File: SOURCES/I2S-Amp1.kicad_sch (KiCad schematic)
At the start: 37 parts, among them P10 CONN_01X02, P17 TST, P24 TST, P25 TST, P26 TST, P9 CONN_01X02, U3 SN74LVC14ADG4, U4 TAS5760MDCAR

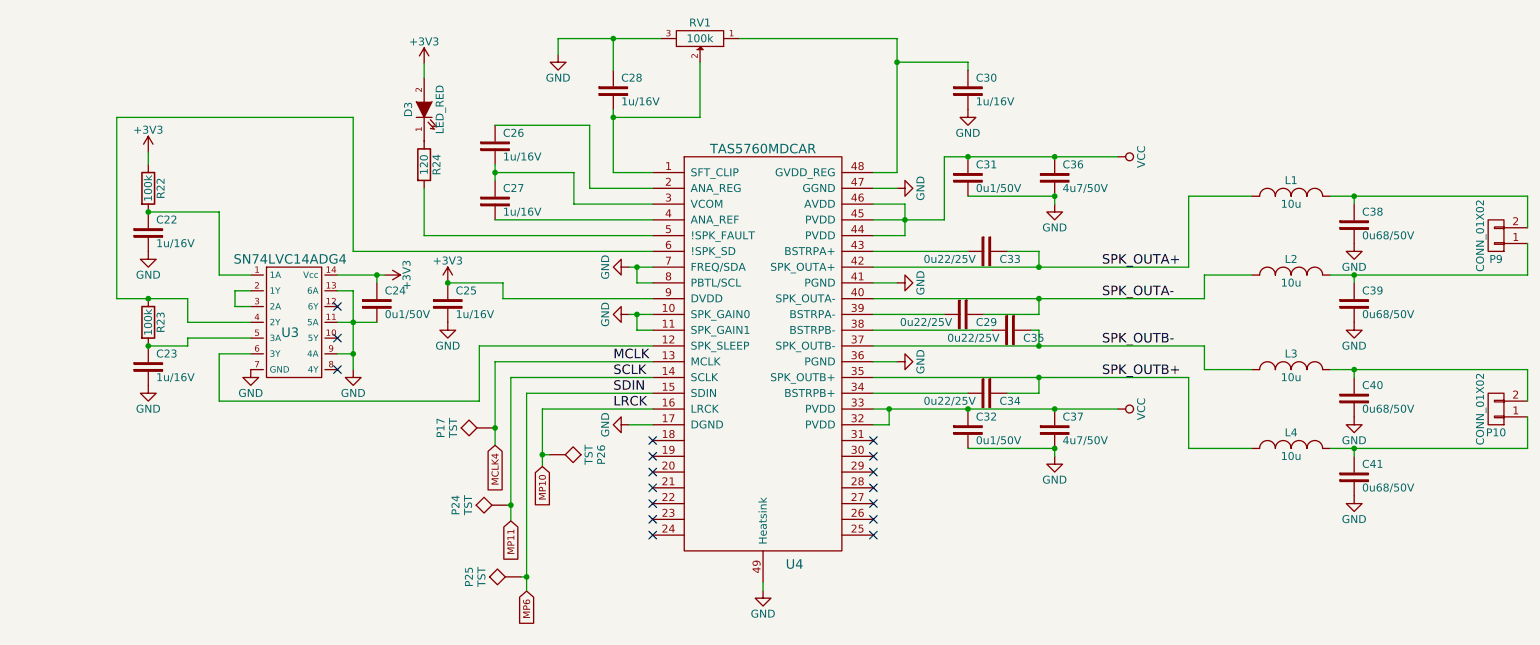
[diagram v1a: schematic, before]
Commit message: Removed redundant 7414 and pot, rerouted a bit.
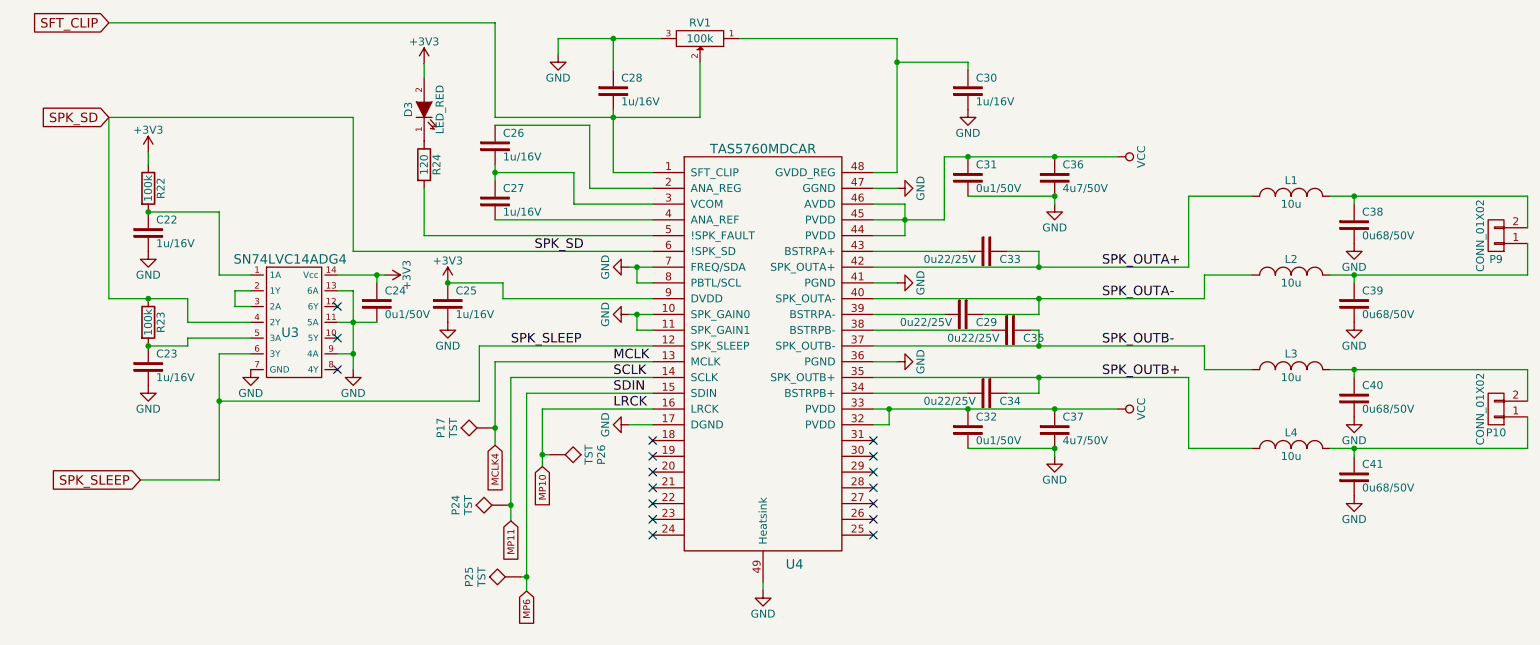
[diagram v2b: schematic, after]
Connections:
- net SFT_CLIP: now reaches C28.2, RV1.2, U4.1 (SFT_CLIP)
- net SPK_SD: now reaches R23.1, U3.4 (2Y), U4.6 (!SPK_SD)
- net SPK_SLEEP: now reaches U3.6 (3Y), U4.12 (SPK_SLEEP)
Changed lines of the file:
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@@
   (junction (at 190.5 81.28) (diameter 0) (color 0 0 0 0)
+  )
+  (junction (at 58.42 85.09) (diameter 0) (color 0 0 0 0)
   )
   (junction (at 80.01 77.47) (diameter 0) (color 0 0 0 0)
@@
     (stroke (width 0) (type default))
   )
+  (wire (pts (xy 40.64 24.13) (xy 102.87 24.13))
+    (stroke (width 0) (type default))
+  )
   (wire (pts (xy 167.64 26.67) (xy 167.64 30.48))
     (stroke (width 0) (type default))
@@
     (stroke (width 0) (type default))
   )
+  (wire (pts (xy 102.87 39.37) (xy 121.92 39.37))
+    (stroke (width 0) (type default))
+  )
   (wire (pts (xy 179.07 83.82) (xy 163.83 83.82))
     (stroke (width 0) (type default))
@@
     (stroke (width 0) (type default))
   )
+  (wire (pts (xy 58.42 97.79) (xy 58.42 85.09))
+    (stroke (width 0) (type default))
+  )
   (wire (pts (xy 175.26 45.72) (xy 179.07 45.72))
     (stroke (width 0) (type default))
@@
     (stroke (width 0) (type default))
   )
-  (wire (pts (xy 41.91 68.58) (xy 41.91 39.37))
+  (wire (pts (xy 40.64 68.58) (xy 40.64 39.37))
     (stroke (width 0) (type default))
   )
@@
     (stroke (width 0) (type default))
   )
-  (wire (pts (xy 41.91 68.58) (xy 46.99 68.58))
+  (wire (pts (xy 40.64 68.58) (xy 46.99 68.58))
     (stroke (width 0) (type default))
   )
@@
     (stroke (width 0) (type default))
   )
+  (wire (pts (xy 102.87 24.13) (xy 102.87 39.37))
+    (stroke (width 0) (type default))
+  )
   (wire (pts (xy 102.87 55.88) (xy 128.27 55.88))
     (stroke (width 0) (type default))
@@
     (stroke (width 0) (type default))
   )
-  (wire (pts (xy 41.91 39.37) (xy 80.01 39.37))
+  (wire (pts (xy 40.64 39.37) (xy 80.01 39.37))
     (stroke (width 0) (type default))
   )
@@
     (stroke (width 0) (type default))
   )
+  (wire (pts (xy 45.72 97.79) (xy 58.42 97.79))
+    (stroke (width 0) (type default))
+  )
   (wire (pts (xy 241.3 64.77) (xy 241.3 66.04))
     (stroke (width 0) (type default))
@@
     (stroke (width 0) (type default))
   )
-  (label "SPK_OUTB-" (at 200.66 76.2 0)
-    (effects (font (size 1.524 1.524)) (justify left bottom))
-  )
-  (label "SDIN" (at 121.92 83.82 0)
-    (effects (font (size 1.524 1.524)) (justify left bottom))
-  )
-  (label "SPK_OUTA-" (at 200.66 68.58 0)
-    (effects (font (size 1.524 1.524)) (justify left bottom))
-  )
-  (label "SPK_OUTA+" (at 200.66 63.5 0)
-    (effects (font (size 1.524 1.524)) (justify left bottom))
-  )
-  (label "SCLK" (at 121.92 81.28 0)
-    (effects (font (size 1.524 1.524)) (justify left bottom))
-  )
-  (label "LRCK" (at 121.92 86.36 0)
-    (effects (font (size 1.524 1.524)) (justify left bottom))
-  )
-  (label "SPK_OUTB+" (at 200.66 81.28 0)
-    (effects (font (size 1.524 1.524)) (justify left bottom))
-  )
-  (label "MCLK" (at 121.92 78.74 0)
+  (label "SPK_OUTB-" (at 200.66 76.2 0) (fields_autoplaced)
+    (effects (font (size 1.524 1.524)) (justify left bottom))
+  )
+  (label "SDIN" (at 121.92 83.82 0) (fields_autoplaced)
+    (effects (font (size 1.524 1.524)) (justify left bottom))
+  )
+  (label "SPK_SD" (at 109.22 60.96 0) (fields_autoplaced)
+    (effects (font (size 1.524 1.524)) (justify left bottom))
+  )
+  (label "SPK_SLEEP" (at 105.41 76.2 0) (fields_autoplaced)
+    (effects (font (size 1.524 1.524)) (justify left bottom))
+  )
+  (label "SPK_OUTA-" (at 200.66 68.58 0) (fields_autoplaced)
+    (effects (font (size 1.524 1.524)) (justify left bottom))
+  )
+  (label "SPK_OUTA+" (at 200.66 63.5 0) (fields_autoplaced)
+    (effects (font (size 1.524 1.524)) (justify left bottom))
+  )
+  (label "SCLK" (at 121.92 81.28 0) (fields_autoplaced)
+    (effects (font (size 1.524 1.524)) (justify left bottom))
+  )
+  (label "LRCK" (at 121.92 86.36 0) (fields_autoplaced)
+    (effects (font (size 1.524 1.524)) (justify left bottom))
+  )
+  (label "SPK_OUTB+" (at 200.66 81.28 0) (fields_autoplaced)
+    (effects (font (size 1.524 1.524)) (justify left bottom))
+  )
+  (label "MCLK" (at 121.92 78.74 0) (fields_autoplaced)
     (effects (font (size 1.524 1.524)) (justify left bottom))
   )
@@
     )
   )
+  (global_label "SPK_SLEEP" (shape input) (at 45.72 97.79 180) (fields_autoplaced)
+    (effects (font (size 1.524 1.524)) (justify right))
+    (property "Intersheetrefs" "${INTERSHEET_REFS}" (at 30.2958 97.79 0)
+      (effects (font (size 1.27 1.27)) (justify right) hide)
+    )
+  )
+  (global_label "SFT_CLIP" (shape input) (at 40.64 24.13 180) (fields_autoplaced)
+    (effects (font (size 1.524 1.524)) (justify right))
+    (property "Intersheetrefs" "${INTERSHEET_REFS}" (at 27.7559 24.13 0)
+      (effects (font (size 1.27 1.27)) (justify right) hide)
+    )
+  )
+  (global_label "SPK_SD" (shape input) (at 40.64 39.37 180) (fields_autoplaced)
+    (effects (font (size 1.524 1.524)) (justify right))
+    (property "Intersheetrefs" "${INTERSHEET_REFS}" (at 29.2073 39.37 0)
+      (effects (font (size 1.27 1.27)) (justify right) hide)
+    )
+  )

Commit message: Removed ArduinoPort, Changed Power Supply. Rerouting and stuff.
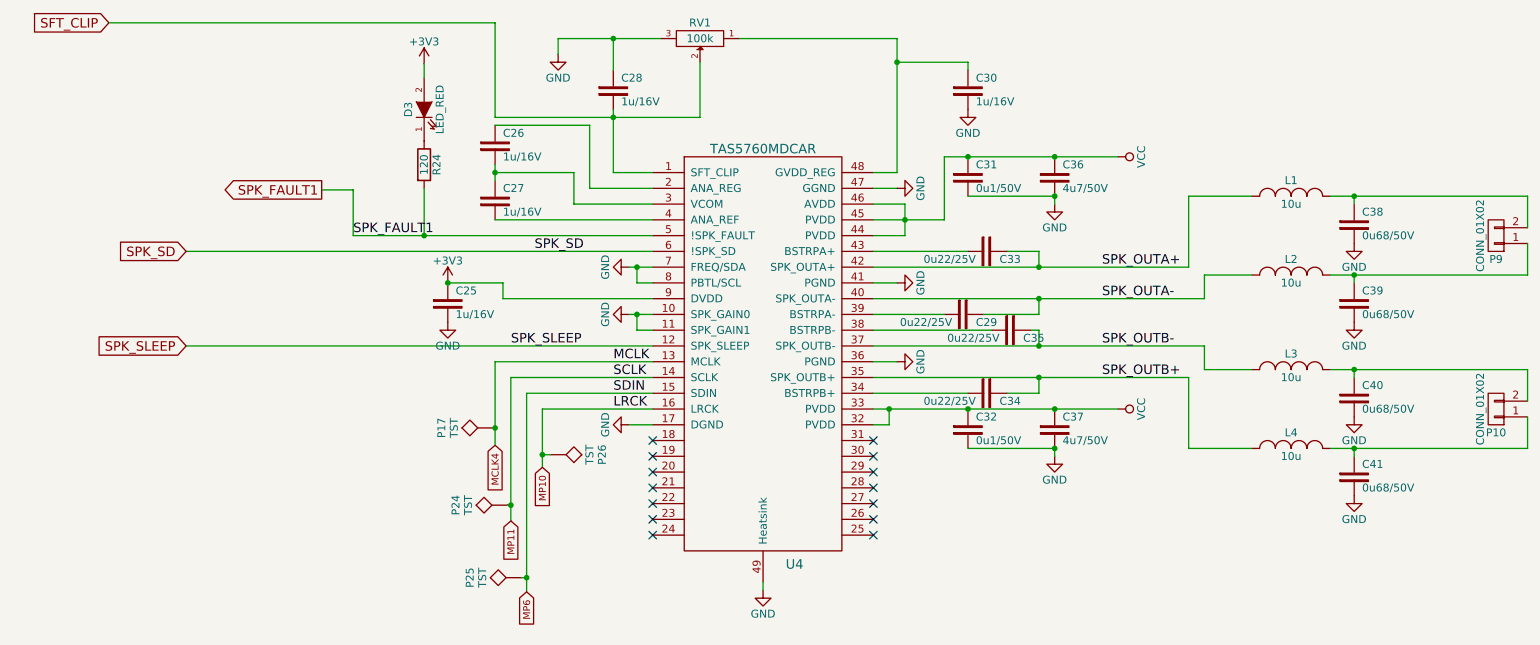
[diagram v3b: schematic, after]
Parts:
- removed C22, C23: 1u/16V, fdsp_capacitor:C_1206_HandSoldering, symbol MyLibrary:Capacitor
- removed C24: 0u1/50V, fdsp_capacitor:C_1206_HandSoldering, symbol MyLibrary:Capacitor
- removed R22, R23: 100k, fdsp_resistor:R_1206_HandSoldering, symbol smd_aio-rescue:R
- removed U3: SN74LVC14ADG4, Housings_SOIC:SOIC-14_3.9x8.7mm_Pitch1.27mm, symbol MyLibrary:SN74LVC14ADG4
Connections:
- net SPK_FAULT1: now reaches R24.2, U4.5 (!SPK_FAULT)
- no-connect marks 17 -> 14

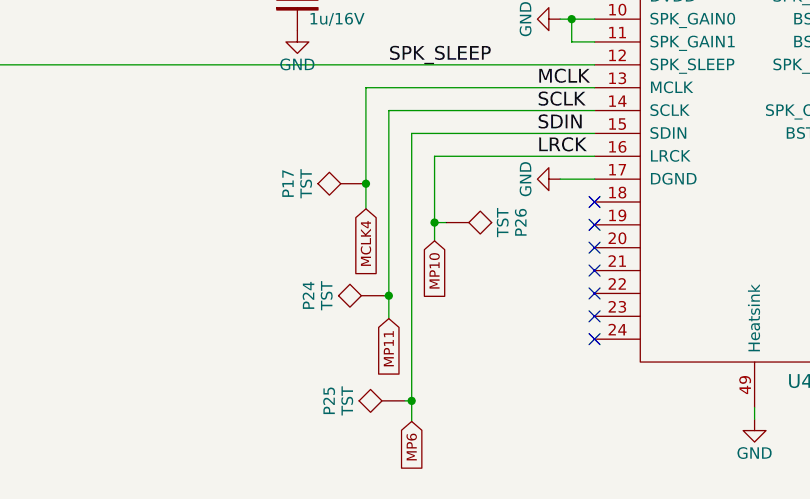
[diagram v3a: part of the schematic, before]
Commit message: Added power down detection.
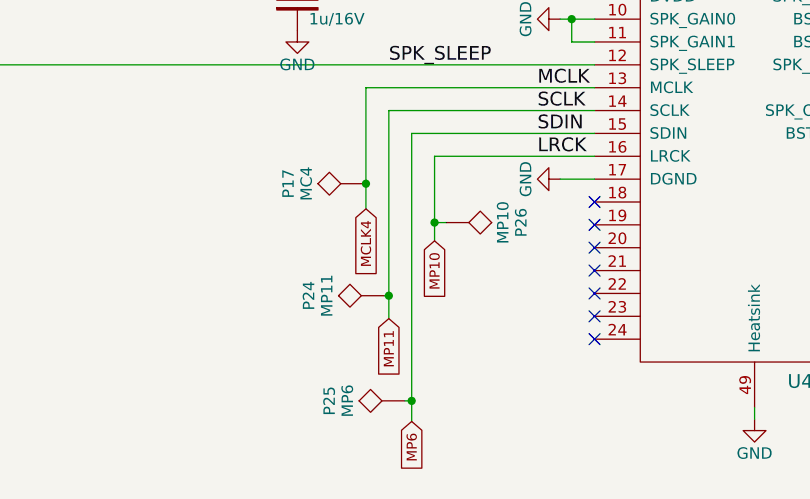
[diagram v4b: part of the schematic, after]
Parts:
- P17: value TST -> MC4
- P24: value TST -> MP11
- P25: value TST -> MP6
- P26: value TST -> MP10
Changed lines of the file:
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@@
       (effects (font (size 1.27 1.27)) (justify bottom))
     )
-    (property "Value" "TST" (at 96.266 89.408 0)
+    (property "Value" "MC4" (at 96.266 89.408 0)
       (effects (font (size 1.27 1.27)))
     )
@@
       (effects (font (size 1.27 1.27)) (justify bottom))
     )
-    (property "Value" "TST" (at 98.552 101.854 0)
+    (property "Value" "MP11" (at 98.552 101.854 0)
       (effects (font (size 1.27 1.27)))
     )
@@
       (effects (font (size 1.27 1.27)) (justify bottom))
     )
-    (property "Value" "TST" (at 100.838 113.538 0)
+    (property "Value" "MP6" (at 100.838 113.538 0)
       (effects (font (size 1.27 1.27)))
     )
@@
       (effects (font (size 1.27 1.27)) (justify bottom))
     )
-    (property "Value" "TST" (at 118.11 93.726 0)
+    (property "Value" "MP10" (at 118.11 93.726 0)
       (effects (font (size 1.27 1.27)))
     )

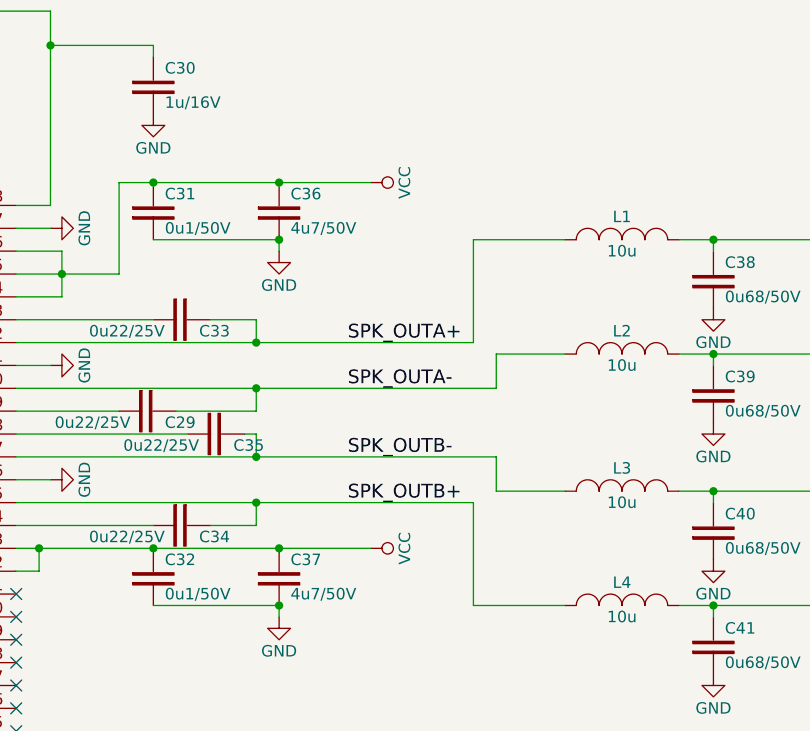
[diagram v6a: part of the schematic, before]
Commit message: Fixed Vin/Vcc issue.
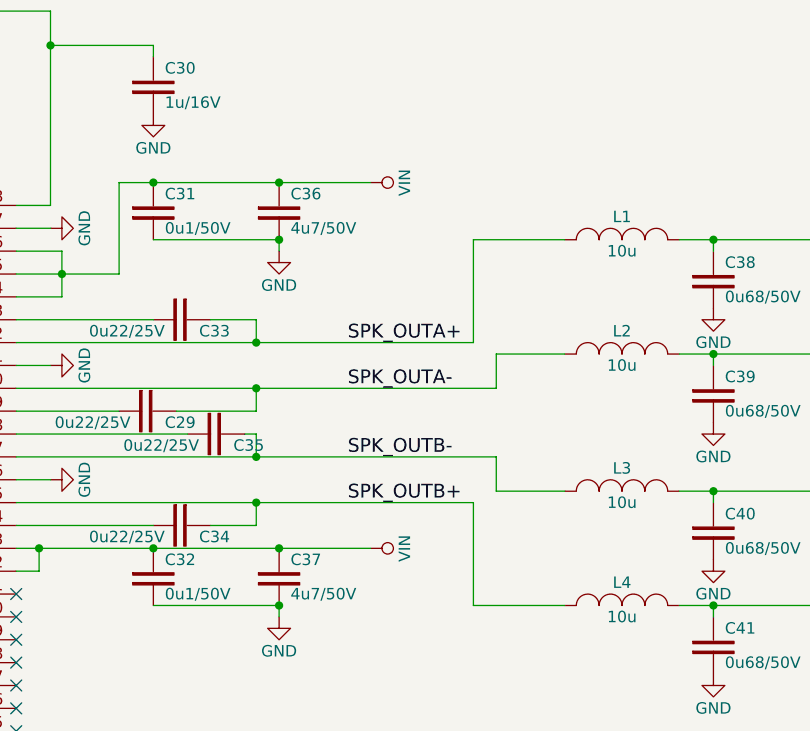
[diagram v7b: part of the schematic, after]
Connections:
- net VCC renamed VIN
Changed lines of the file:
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@@
 			)
 		)
-		(property "Value" "VCC"
+		(property "Value" "VIN"
 			(at 207.01 86.36 0)
 			(effects
@@
 			)
 		)
-		(property "Value" "VCC"
+		(property "Value" "VIN"
 			(at 207.01 45.72 0)
 			(effects
